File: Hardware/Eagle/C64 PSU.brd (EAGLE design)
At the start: 100 x 60 mm, 9 parts

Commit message: Fixed solder pads for trafo
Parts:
- U$1: value TEZTRAFFO -> TEZTRAFO; device traffo:TEZ10/D230/9V -> trafo:TEZ10/D230/9V
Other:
- board text added: "Commodore 64 PSU v1.1 Copyright (c) 2018 Retro Commodore http://www.retro-commodore.eu/diy-open-source-stuff/ Solder Side"
- board text removed: "Commodore 64 PSU v1.0 Copyright (c) 2018 Retro Commodore http://www.retro-commodore.eu/diy-open-source-stuff/ Solder Side"
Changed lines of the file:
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@@
 <?xml version="1.0" encoding="utf-8"?>
 <!DOCTYPE eagle SYSTEM "eagle.dtd">
-<eagle version="9.1.3">
+<eagle version="9.2.2">
 <drawing>
 <settings>
@@
 <text x="5.461" y="22.479" size="1.778" layer="25" rot="R90">200mA T</text>
 <hole x="5" y="43" drill="5"/>
-<text x="21" y="22" size="1.9" layer="26">Commodore 64 PSU v1.0
+<text x="21" y="22" size="1.9" layer="26">Commodore 64 PSU v1.1
 Copyright (c) 2018 Retro Commodore
 http://www.retro-commodore.eu/diy-open-source-stuff/
@@
 </autorouter>
 <elements>
-<element name="U$1" library="traffo" package="TEZ10/D230/9V" value="TEZTRAFFO" x="53.086" y="16.129" smashed="yes" rot="R90"/>
+<element name="U$1" library="trafo" package="TEZ10/D230/9V" value="TEZTRAFO" x="53.086" y="16.129" smashed="yes" rot="R90"/>
 <element name="F1" library="fuse" library_urn="urn:adsk.eagle:library:233" package="SH22,5" package3d_urn="urn:adsk.eagle:package:14059/1" value="250mA T" x="4.92" y="27.33" smashed="yes" rot="R90">
 <attribute name="MF" value="" x="4.92" y="27.33" size="1.778" layer="27" rot="R90" display="off"/>

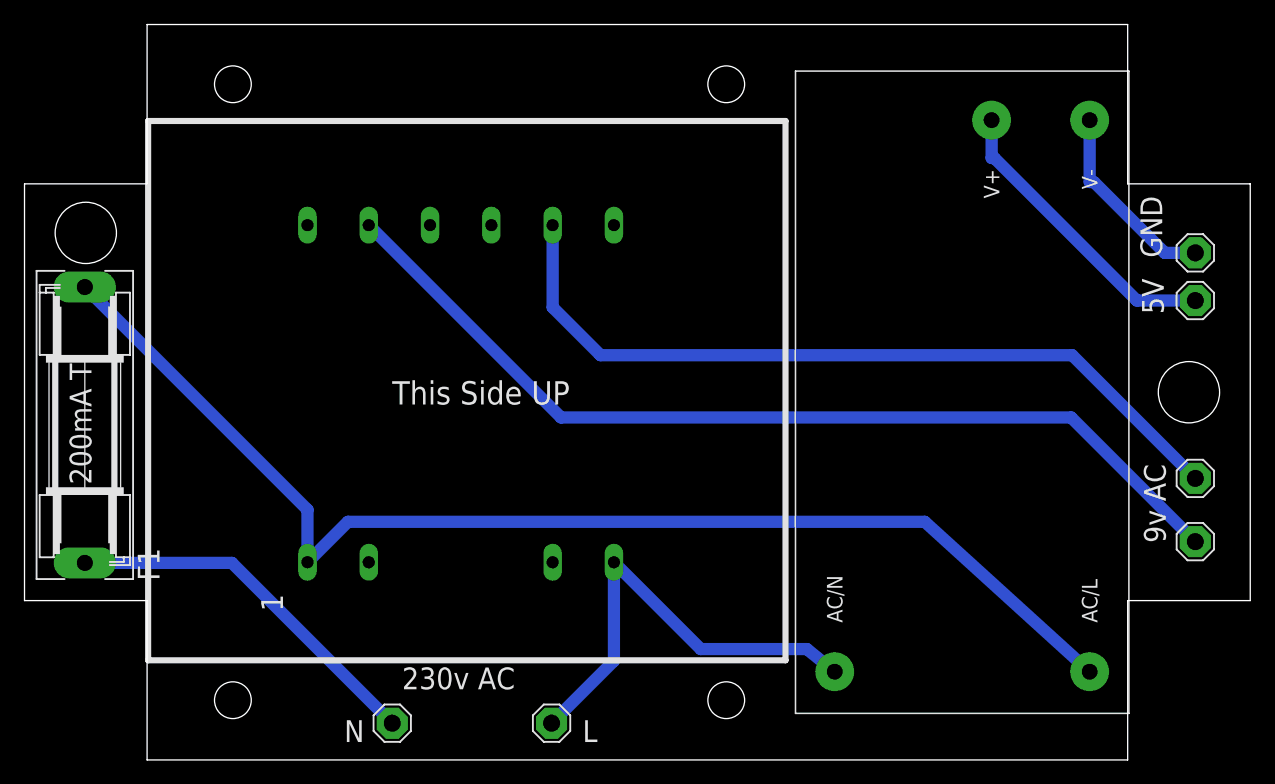
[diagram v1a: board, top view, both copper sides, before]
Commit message: Small updates based on ycombinator comments
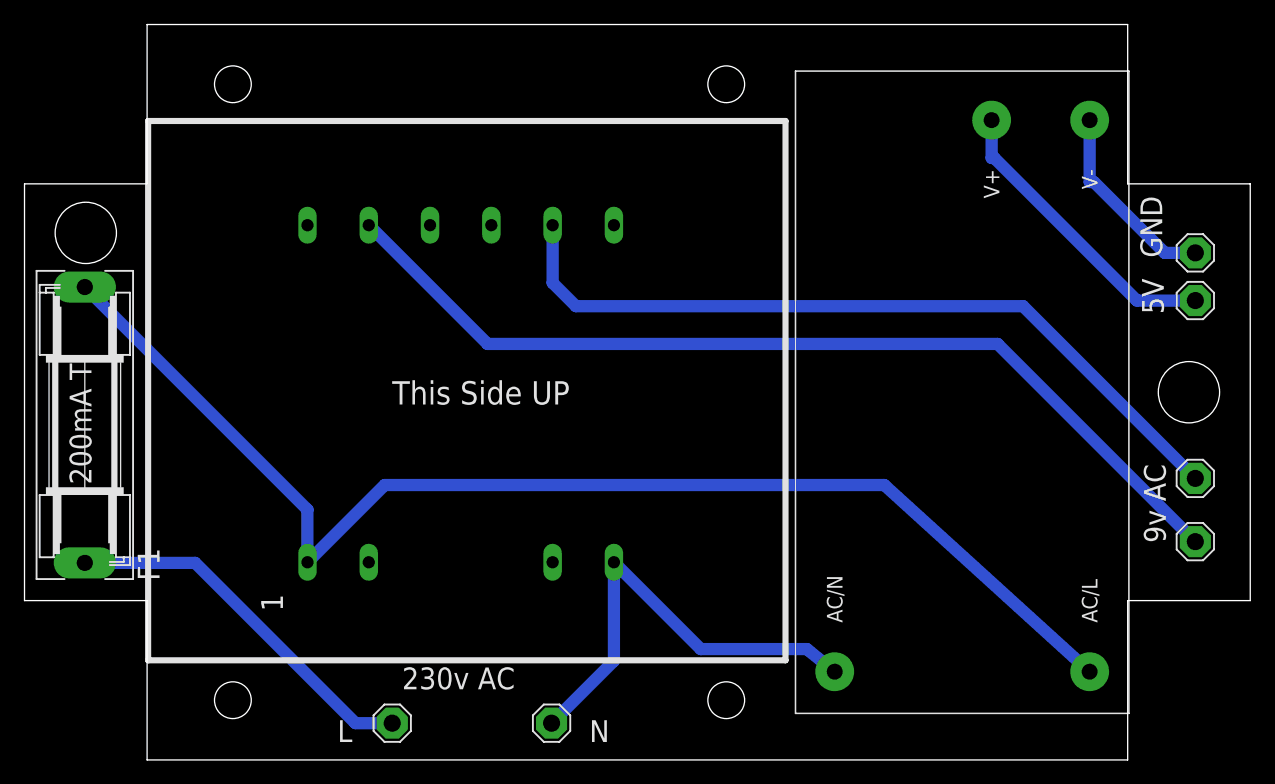
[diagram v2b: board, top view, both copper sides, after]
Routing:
- net N$1: track 100.8 -> 102.3 mm
- net N$4: track 64.9 -> 63.7 mm
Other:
- board text added: "Commodore 64 PSU v1.2 Copyright (c) 2018 Retro Commodore http://www.retro-commodore.eu/diy-open-source-stuff/ Solder Side"
- board text removed: "Commodore 64 PSU v1.1 Copyright (c) 2018 Retro Commodore http://www.retro-commodore.eu/diy-open-source-stuff/ Solder Side"
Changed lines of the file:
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@@
 <text x="40.019" y="7.543" size="1.778" layer="25" rot="R180">230v AC</text>
 <hole x="17" y="4.875" drill="3"/>
-<text x="45.527" y="1.463" size="1.778" layer="25">L</text>
-<text x="26.083" y="1.463" size="1.778" layer="25">N</text>
+<text x="25.527" y="1.463" size="1.778" layer="25">L</text>
+<text x="46.083" y="1.463" size="1.778" layer="25">N</text>
 <hole x="57.25" y="4.875" drill="3"/>
 <hole x="17" y="55.125" drill="3"/>
@@
 <text x="5.461" y="22.479" size="1.778" layer="25" rot="R90">200mA T</text>
 <hole x="5" y="43" drill="5"/>
-<text x="21" y="22" size="1.9" layer="26">Commodore 64 PSU v1.1
+<text x="21" y="22" size="1.9" layer="26">Commodore 64 PSU v1.2
 Copyright (c) 2018 Retro Commodore
 http://www.retro-commodore.eu/diy-open-source-stuff/
@@
 <contactref element="U$1" pad="P1"/>
 <contactref element="U$2" pad="AC/L"/>
-<wire x1="86.9" y1="7.2" x2="86.057" y2="7.62" width="1" layer="1"/>
-<wire x1="86.9" y1="7.2" x2="73.447" y2="19.43" width="1" layer="16"/>
-<wire x1="73.447" y1="19.43" x2="26.387" y2="19.43" width="1" layer="16"/>
-<wire x1="23.086" y1="16.129" x2="26.387" y2="19.43" width="1" layer="16"/>
+<wire x1="86.9" y1="7.2" x2="70.147" y2="22.43" width="1" layer="16"/>
+<wire x1="70.147" y1="22.43" x2="29.387" y2="22.43" width="1" layer="16"/>
+<wire x1="23.086" y1="16.129" x2="29.387" y2="22.43" width="1" layer="16"/>
 <wire x1="4.92" y1="38.5822" x2="23.086" y2="20.4162" width="1" layer="16"/>
 <wire x1="23.086" y1="20.4162" x2="23.086" y2="16.129" width="1" layer="16"/>
@@
 <contactref element="F1" pad="1"/>
 <contactref element="LSP2" pad="MP"/>
-<wire x1="30" y1="3" x2="16.9222" y2="16.0778" width="1" layer="16"/>
-<wire x1="16.9222" y1="16.0778" x2="4.92" y2="16.0778" width="1" layer="16"/>
+<wire x1="30" y1="3" x2="27" y2="3" width="1" layer="16"/>
+<wire x1="27" y1="3" x2="13.9222" y2="16.0778" width="1" layer="16"/>
+<wire x1="13.9222" y1="16.0778" x2="4.92" y2="16.0778" width="1" layer="16"/>
 </signal>
 <signal name="N$4">
 <contactref element="U$1" pad="S8"/>
 <contactref element="LSP6" pad="MP"/>
-<wire x1="85.47" y1="33.02" x2="95.52" y2="22.97" width="1" layer="16"/>
-<wire x1="43.086" y1="36.924" x2="46.99" y2="33.02" width="1" layer="16"/>
-<wire x1="46.99" y1="33.02" x2="85.47" y2="33.02" width="1" layer="16"/>
-<wire x1="43.086" y1="43.629" x2="43.086" y2="36.924" width="1" layer="16"/>
+<wire x1="81.47" y1="37.02" x2="95.52" y2="22.97" width="1" layer="16"/>
+<wire x1="43.086" y1="38.924" x2="44.99" y2="37.02" width="1" layer="16"/>
+<wire x1="44.99" y1="37.02" x2="81.47" y2="37.02" width="1" layer="16"/>
+<wire x1="43.086" y1="43.629" x2="43.086" y2="38.924" width="1" layer="16"/>
 </signal>
 <signal name="N$5">
 <contactref element="U$1" pad="S11"/>
 <contactref element="LSP5" pad="MP"/>
-<wire x1="43.775" y1="27.94" x2="28.086" y2="43.629" width="1" layer="16"/>
-<wire x1="95.52" y1="17.81" x2="85.39" y2="27.94" width="1" layer="16"/>
-<wire x1="85.39" y1="27.94" x2="43.775" y2="27.94" width="1" layer="16"/>
+<wire x1="37.775" y1="33.94" x2="28.086" y2="43.629" width="1" layer="16"/>
+<wire x1="95.52" y1="17.81" x2="79.39" y2="33.94" width="1" layer="16"/>
+<wire x1="79.39" y1="33.94" x2="37.775" y2="33.94" width="1" layer="16"/>
 </signal>
 <signal name="N$6">

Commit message: added power led connectors
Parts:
- added PWRLED: 22-23-2021, con-molex:22-23-2021
- added R1: (no value), rcl:0207/10
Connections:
- new net N$8: PWRLED.1, R1.2
- net N$6: now also R1.1
- net N$7: now also PWRLED.2
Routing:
- net N$7: track 24.5 -> 36.1 mm
- net N$6: track 16.1 -> 21.9 mm
- net N$8: track 0.00 -> 4.65 mm
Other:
- board text added: "+"
- board text added: "-"
- board text added: "Commodore 64 PSU v1.3 Copyright (c) 2018-2019 Retro Commodore http://www.retro-commodore.eu/diy-open-source-stuff/ Solder Side"
- board text removed: "Commodore 64 PSU v1.2 Copyright (c) 2018 Retro Commodore http://www.retro-commodore.eu/diy-open-source-stuff/ Solder Side"
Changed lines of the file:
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@@
 <?xml version="1.0" encoding="utf-8"?>
 <!DOCTYPE eagle SYSTEM "eagle.dtd">
-<eagle version="9.2.2">
+<eagle version="9.3.2">
 <drawing>
 <settings>
@@
 <text x="5.461" y="22.479" size="1.778" layer="25" rot="R90">200mA T</text>
 <hole x="5" y="43" drill="5"/>
-<text x="21" y="22" size="1.9" layer="26">Commodore 64 PSU v1.2
-Copyright (c) 2018 Retro Commodore
+<text x="21" y="22" size="1.9" layer="26">Commodore 64 PSU v1.3
+Copyright (c) 2018-2019 Retro Commodore
 http://www.retro-commodore.eu/diy-open-source-stuff/
 Solder Side</text>
 <text x="30" y="29" size="1.9" layer="25">This Side UP</text>
+<text x="67" y="57" size="1.778" layer="21">+</text>
+<text x="74" y="57" size="1.778" layer="21">-</text>
 </plain>
 <attributes>
@@
 <attribute name="VALUE" x="95.52" y="23.351" size="0.0254" layer="27"/>
 </element>
+<element name="R1" library="rcl" library_urn="urn:adsk.eagle:library:334" package="0207/10" package3d_urn="urn:adsk.eagle:package:23491/2" value="" x="82" y="58" smashed="yes" rot="R180">
+<attribute name="NAME" x="85.048" y="56.476" size="1.27" layer="25" ratio="10" rot="R180"/>
+<attribute name="SPICEPREFIX" value="R" x="82" y="58" size="1.778" layer="27" rot="R180" display="off"/>
+<attribute name="VALUE" x="84.2606" y="58.635" size="1.27" layer="27" ratio="10" rot="R180"/>
+</element>
+<element name="PWRLED" library="con-molex" package="22-23-2021" package3d_urn="urn:adsk.eagle:package:8078633/1" value="22-23-2021" x="71" y="58" smashed="yes" rot="R180">
+<attribute name="MF" value="MOLEX" x="71" y="58" size="1.778" layer="27" rot="R180" display="off"/>
+<attribute name="MPN" value="22-23-2021" x="71" y="58" size="1.778" layer="27" rot="R180" display="off"/>
+<attribute name="NAME" x="66.936" y="58.381" size="1.016" layer="25" ratio="10" rot="R180"/>
+<attribute name="OC_FARNELL" value="1462926" x="71" y="58" size="1.778" layer="27" rot="R180" display="off"/>
+<attribute name="OC_NEWARK" value="25C3832" x="71" y="58" size="1.778" layer="27" rot="R180" display="off"/>
+</element>
 </elements>
 <signals>
@@
 <wire x1="95.52" y1="41.37" x2="93.028" y2="41.37" width="1" layer="16"/>
 <wire x1="93.028" y1="41.37" x2="87.267" y2="47.131" width="1" layer="16"/>
+<contactref element="R1" pad="1"/>
+<wire x1="86.9" y1="52.2" x2="86.9" y2="57.82" width="0.1524" layer="16"/>
+<wire x1="86.9" y1="57.82" x2="87.08" y2="58" width="0.1524" layer="16"/>
 </signal>
 <signal name="N$7">
@@
 <wire x1="79.14" y1="49.092" x2="78.9" y2="49.11188125" width="1" layer="16"/>
 <wire x1="78.9" y1="49.11188125" x2="78.9" y2="52.2" width="1" layer="16"/>
+<wire x1="78.9" y1="52.2" x2="75.53" y2="52.2" width="0.1524" layer="16"/>
+<wire x1="75.53" y1="52.2" x2="73.865" y2="53.865" width="0.1524" layer="16"/>
+<wire x1="73.865" y1="53.865" x2="69.73" y2="58" width="0.1524" layer="16"/>
+<contactref element="PWRLED" pad="2"/>
+</signal>
+<signal name="N$8">
+<contactref element="R1" pad="2"/>
+<wire x1="72.27" y1="58" x2="76.92" y2="58" width="0.1524" layer="16"/>
+<contactref element="PWRLED" pad="1"/>
 </signal>
 </signals>

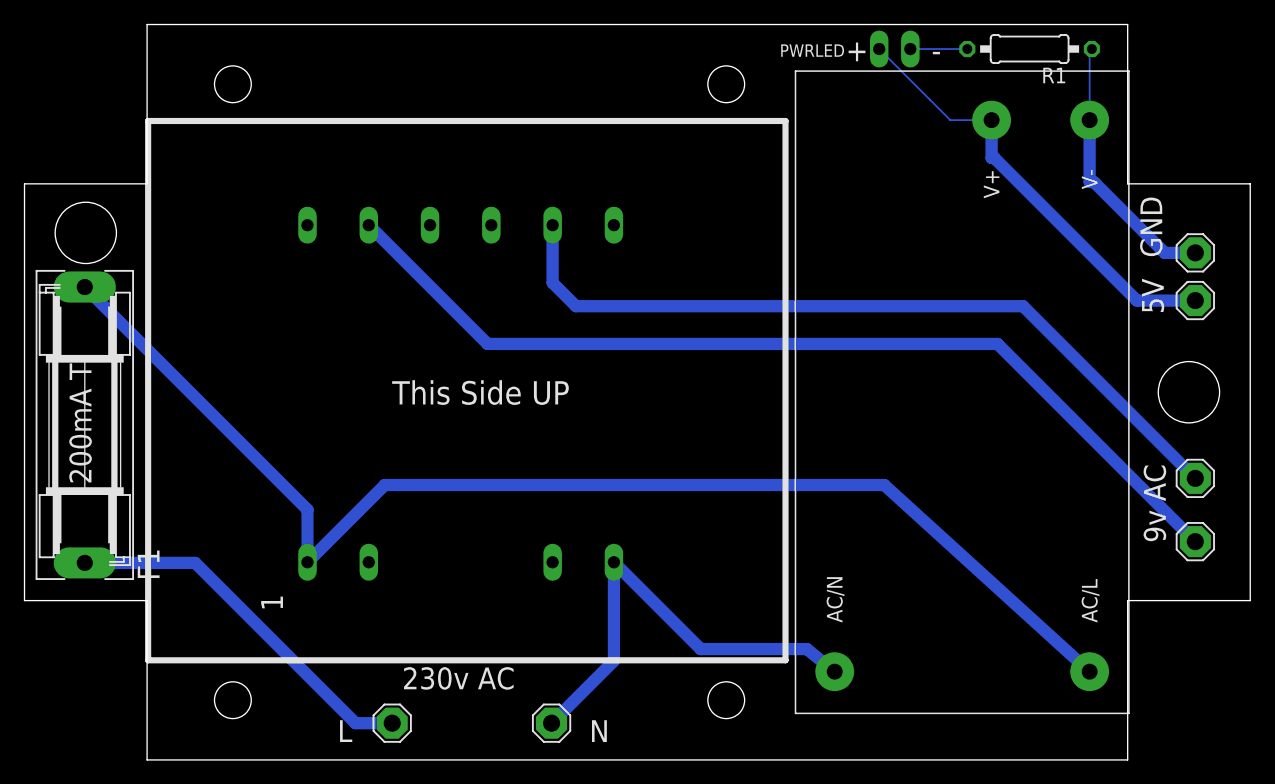
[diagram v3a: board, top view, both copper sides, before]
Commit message: Improved traces
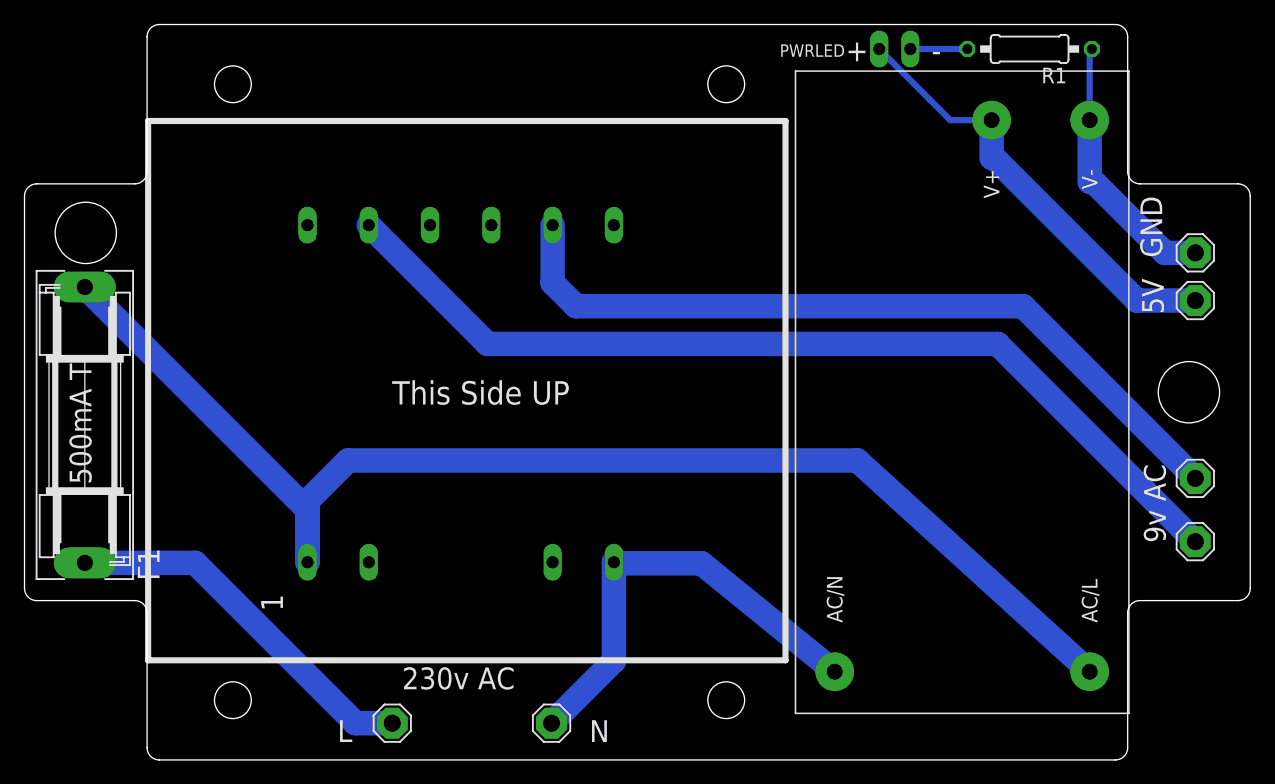
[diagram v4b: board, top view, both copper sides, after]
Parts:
- F1: value 250mA T -> 500mA T
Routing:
- net N$1: track 102.3 -> 106.8 mm
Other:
- outline, holes or cut-outs redrawn
- board text added: "500mA T"
- board text added: "Commodore 64 PSU v1.4 Copyright (c) 2018-2019 Retro Commodore http://www.retro-commodore.eu/diy-open-source-stuff/ Solder Side"
- board text removed: "200mA T"
- board text removed: "Commodore 64 PSU v1.3 Copyright (c) 2018-2019 Retro Commodore http://www.retro-commodore.eu/diy-open-source-stuff/ Solder Side"
